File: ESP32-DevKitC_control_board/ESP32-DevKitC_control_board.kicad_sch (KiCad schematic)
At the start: 1 part, among them U1 ESP32-DevKitC

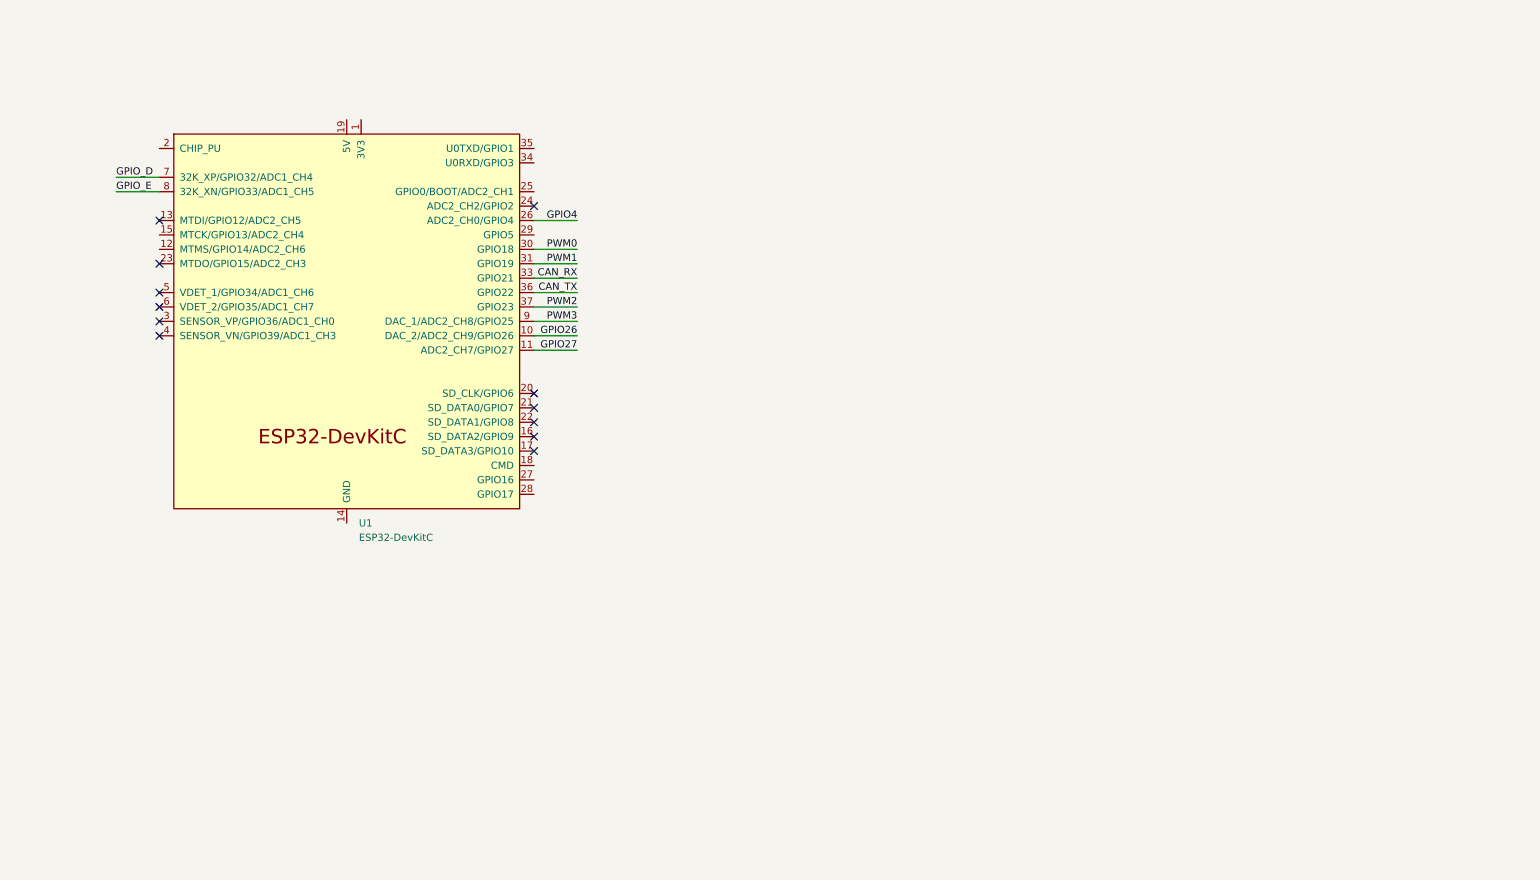
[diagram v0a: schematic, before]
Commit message: ESP32基板　回路図・フットプリント完成
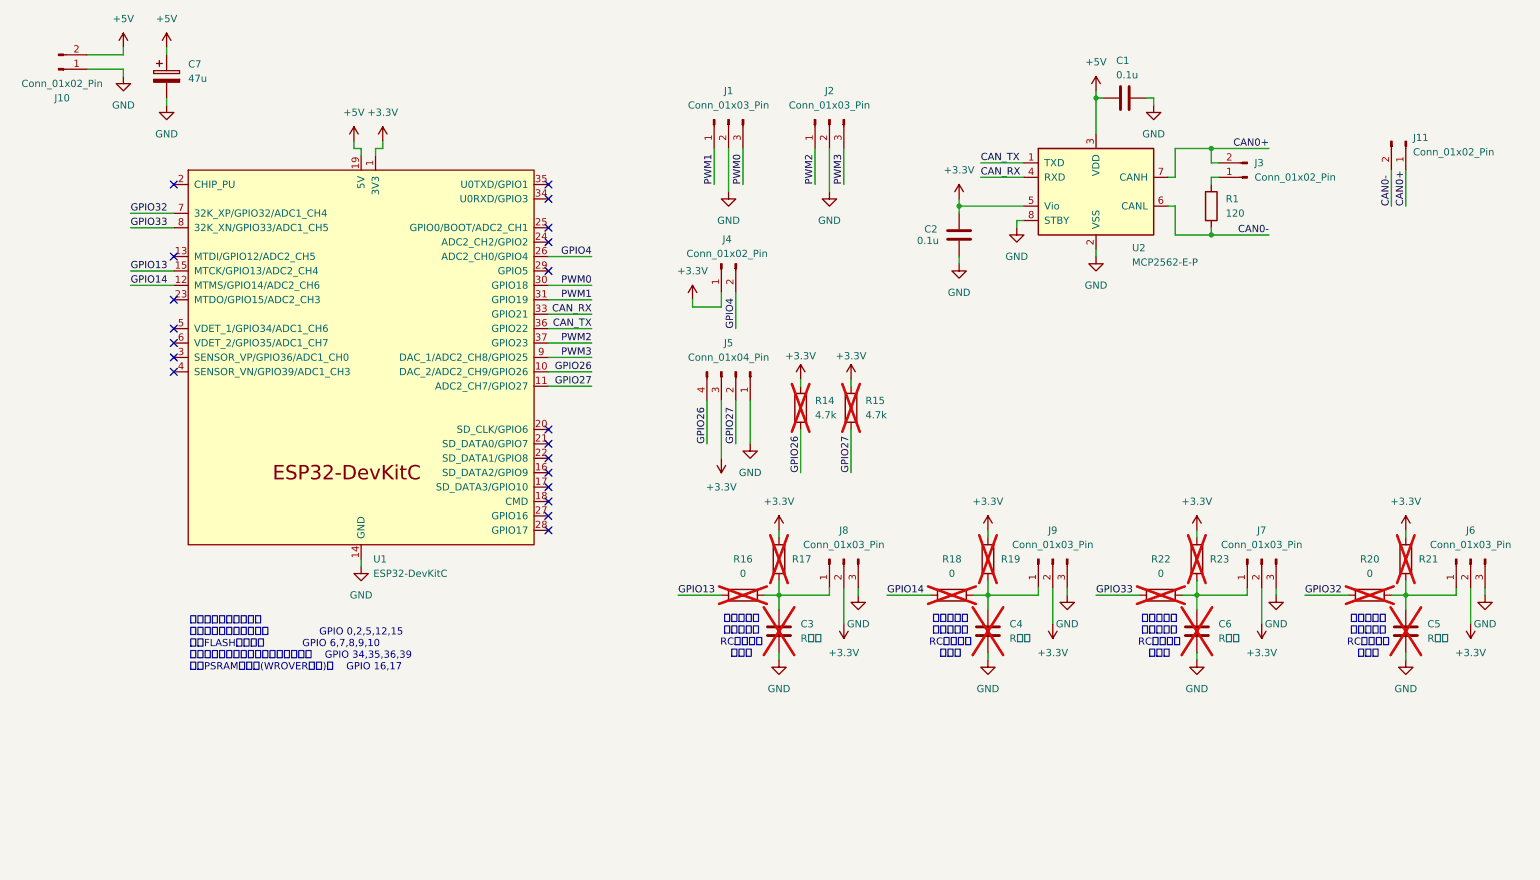
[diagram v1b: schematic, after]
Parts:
- added C1, C2: 0.1u, Capacitor_THT:C_Disc_D4.3mm_W1.9mm_P5.00mm, symbol Device:C
- added C3, C4, C5, C6: R兼用, Capacitor_THT:C_Disc_D3.8mm_W2.6mm_P2.50mm, symbol Device:C
- added C7: 47u, Capacitor_THT:CP_Radial_D6.3mm_P2.50mm, symbol Device:C_Polarized
- added J1, J2: Conn_01x03_Pin, OU_connector:S03B-PASK-2, symbol Connector:Conn_01x03_Pin
- added J10, J11, J4: Conn_01x02_Pin, OU_connector:DF1E-2P-2.5DS, symbol Connector:Conn_01x02_Pin
- added J3: Conn_01x02_Pin, Connector_PinHeader_2.54mm:PinHeader_1x02_P2.54mm_Vertical, symbol Connector:Conn_01x02_Pin
- added J5: Conn_01x04_Pin, OU_connector:DF1EC-4P-2.5DSA, symbol Connector:Conn_01x04_Pin
- added J6, J7, J8, J9: Conn_01x03_Pin, Connector_PinHeader_2.54mm:PinHeader_1x03_P2.54mm_Vertical, symbol Connector:Conn_01x03_Pin
- added R1: 120, Resistor_THT:R_Axial_DIN0204_L3.6mm_D1.6mm_P5.08mm_Horizontal, symbol Device:R
- added R14, R15: 4.7k, Resistor_THT:R_Axial_DIN0207_L6.3mm_D2.5mm_P2.54mm_Vertical, symbol Device:R
- added R16, R18, R20, R22: 0, Resistor_THT:R_Axial_DIN0207_L6.3mm_D2.5mm_P2.54mm_Vertical, symbol Device:R
- added R17, R19, R21, R23: (no value), Resistor_THT:R_Axial_DIN0207_L6.3mm_D2.5mm_P2.54mm_Vertical, symbol Device:R
- added U2: MCP2562-E-P, Package_DIP:DIP-8_W7.62mm, symbol Interface_CAN_LIN:MCP2562-E-P
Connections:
- net CAN_RX: now also U2.4 (RXD)
- net CAN_TX: now also U2.1 (TXD)
- net GPIO26: now also J5.4 (Pin_4), R14.2
- net GPIO27: now also J5.2 (Pin_2), R15.2
- net GPIO4: now also J4.2 (Pin_2)
- net PWM0: now also J1.3 (Pin_3)
- net PWM1: now also J1.1 (Pin_1)
- net PWM2: now also J2.1 (Pin_1)
- net PWM3: now also J2.3 (Pin_3)
- net +3.3V: now reaches U1.1 (3V3)
- net +3.3V: now also C2.2, J4.1 (Pin_1), J5.3 (Pin_3), J6.2 (Pin_2), J7.2 (Pin_2), J8.2 (Pin_2), J9.2 (Pin_2), R14.1, R15.1, R17.2, R19.2, R21.2, R23.2, U2.5 (Vio)
- net GPIO14: now reaches U1.12 (MTMS/GPIO14/ADC2_CH6)
- net GPIO14: now also R18.1
- net GND: now reaches U1.14 (GND), U1.32 (GND), U1.38 (GND)
- net GND: now also C1.2, C2.1, C3.2, C4.2, C5.2, C6.2, C7.2, J1.2 (Pin_2), J10.1 (Pin_1), J2.2 (Pin_2), J5.1 (Pin_1), J6.3 (Pin_3), J7.3 (Pin_3), J8.3 (Pin_3), J9.3 (Pin_3), U2.2 (VSS), U2.8 (STBY)
- net GPIO13: now reaches U1.15 (MTCK/GPIO13/ADC2_CH4)
- net GPIO13: now also R16.1
- net +5V: now reaches U1.19 (5V)
- net +5V: now also C1.1, C7.1, J10.2 (Pin_2), U2.3 (VDD)
- net GPIO_D renamed GPIO32
- net GPIO32: now also R20.1
- net GPIO_E renamed GPIO33
- net GPIO33: now also R22.1
- new net: C6.1, J7.1 (Pin_1), R22.2, R23.1
- new net: C3.1, J8.1 (Pin_1), R16.2, R17.1
- new net: C4.1, J9.1 (Pin_1), R18.2, R19.1
- new net: C5.1, J6.1 (Pin_1), R20.2, R21.1
- new net: J3.1 (Pin_1), R1.1
- new net CAN0+: J11.1 (Pin_1), J3.2 (Pin_2), U2.7 (CANH)
- new net CAN0-: J11.2 (Pin_2), R1.2, U2.6 (CANL)
- no-connect marks 12 -> 20
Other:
- note added: "プルアップ プルダウン RCフィルタ に対応"
- note added: "使わない方がいいピン ブートストラップピン： GPIO 0,2,5,12,15 内蔵FLASHで使用： GPIO 6,7,8,9,10 入力専用・プルアップ・ダウン不可： GPIO 34,35,36,39 外部PSRAMで使用(WROVERのみ)： GPIO 16,17"
- moved on the sheet: U1

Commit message: ESP32基板　PCB途中
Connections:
- net PWM0: now also U1.31 (GPIO19); no longer U1.30 (GPIO18)
- net PWM1: now also U1.30 (GPIO18); no longer U1.31 (GPIO19)

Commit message: ESP32基板　基板完成，ver 0.1
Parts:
- added D4: LED, LED_THT:LED_D5.0mm, symbol Device:LED
- added R12: 1k, Resistor_THT:R_Axial_DIN0207_L6.3mm_D2.5mm_P2.54mm_Vertical, symbol Device:R
- C2: renamed from C1; footprint Capacitor_THT:C_Disc_D4.3mm_W1.9mm_P5.00mm -> Capacitor_THT:C_Disc_D5.0mm_W2.5mm_P2.50mm
- C3: renamed from C2; footprint Capacitor_THT:C_Disc_D4.3mm_W1.9mm_P5.00mm -> Capacitor_THT:C_Disc_D5.0mm_W2.5mm_P2.50mm
- J10: renamed from J7; now not fitted
- J11: renamed from J6; now not fitted
- J7: renamed from J5; footprint OU_connector:DF1EC-4P-2.5DSA -> OU_connector:DF1E-4P-2.5DS
- J8, J9: now not fitted
- R1: footprint Resistor_THT:R_Axial_DIN0204_L3.6mm_D1.6mm_P5.08mm_Horizontal -> Resistor_THT:R_Axial_DIN0207_L6.3mm_D2.5mm_P2.54mm_Vertical
- renumbered C7 to C1, C3 to C4, C4 to C5, C5 to C7, J10 to J1, J1 to J2, J2 to J3, J11 to J4, J3 to J5, J4 to J6, R22 to R10, R20 to R11, R14 to R2, R15 to R3, R17 to R4, R19 to R5, R23 to R6, R21 to R7, R16 to R8, R18 to R9, U2 to U1, U1 to U2
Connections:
- net +5V: now also R12.1
- net CAN_RX: now also U2.30 (GPIO18); no longer U2.33 (GPIO21)
- net CAN_TX: now also U2.31 (GPIO19); no longer U2.36 (GPIO22)
- net GND: now also D4.1 (K)
- net PWM0: now also U2.12 (MTMS/GPIO14/ADC2_CH6); no longer U2.31 (GPIO19)
- net PWM1: now also U2.11 (ADC2_CH7/GPIO27); no longer U2.30 (GPIO18)
- net PWM2: now also U2.9 (DAC_1/ADC2_CH8/GPIO25); no longer U2.37 (GPIO23)
- net PWM3: now also U2.10 (DAC_2/ADC2_CH9/GPIO26); no longer U2.9 (DAC_1/ADC2_CH8/GPIO25)
- net GPIO14 renamed GPIO23
- net GPIO23: now also U2.37 (GPIO23); no longer U2.12 (MTMS/GPIO14/ADC2_CH6)
- net GPIO26 renamed GPIO21
- net GPIO21: now also U2.33 (GPIO21); no longer U2.10 (DAC_2/ADC2_CH9/GPIO26)
- net GPIO27 renamed GPIO22
- net GPIO22: now also U2.36 (GPIO22); no longer U2.11 (ADC2_CH7/GPIO27)
- new net: D4.2 (A), R12.2
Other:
- note added: "5V電源LED"
- moved on the sheet: C1, U2

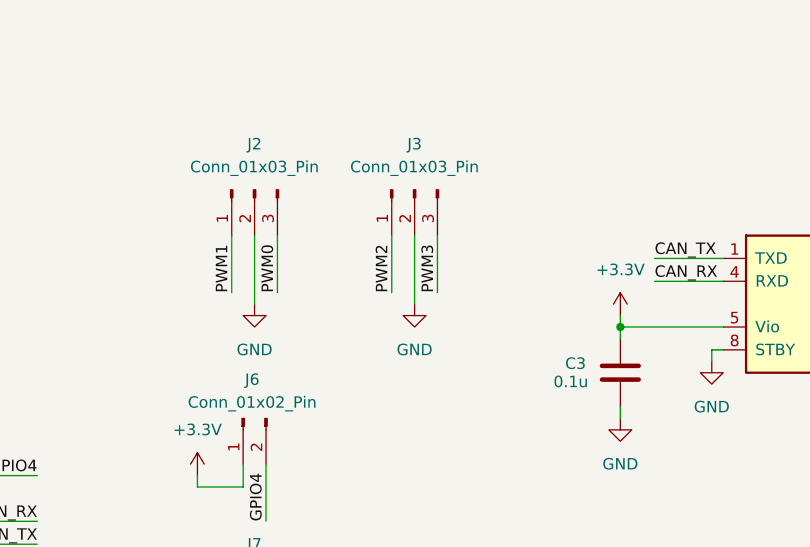
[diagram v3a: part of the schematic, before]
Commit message: ESP32基板　回路図を修正
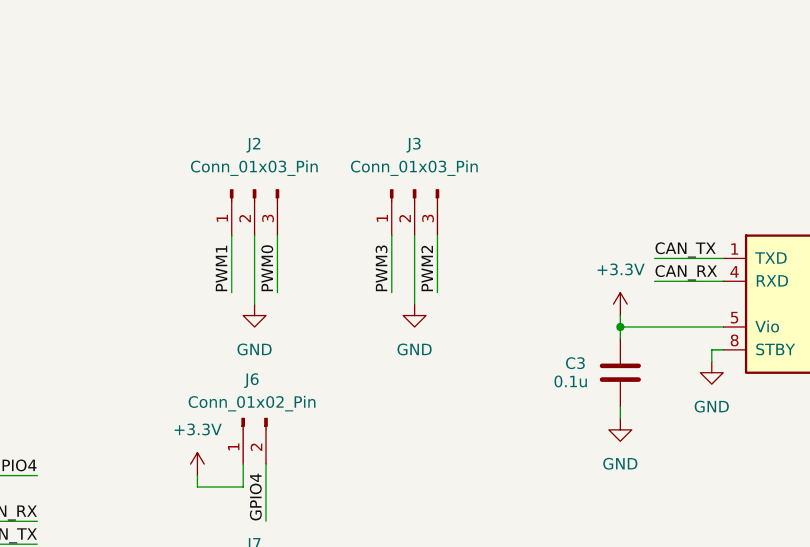
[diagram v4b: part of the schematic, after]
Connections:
- net PWM2: now also J3.3 (Pin_3); no longer J3.1 (Pin_1)
- net PWM3: now also J3.1 (Pin_1); no longer J3.3 (Pin_3)
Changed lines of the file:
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@@
-	(wire
-		(pts
-			(xy 154.94 44.45) (xy 154.94 38.1)
-		)
-		(stroke
-			(width 0)
-			(type default)
-		)
-	)
 	(wire
 		(pts
@@
 	(wire
 		(pts
+			(xy 154.94 38.1) (xy 154.94 44.45)
+		)
+		(stroke
+			(width 0)
+			(type default)
+		)
+	)
+	(wire
+		(pts
 			(xy 148.59 114.3) (xy 148.59 116.84)
 		)
@@
 	(wire
 		(pts
+			(xy 160.02 44.45) (xy 160.02 38.1)
+		)
+		(stroke
+			(width 0)
+			(type default)
+		)
+	)
+	(wire
+		(pts
 			(xy 236.22 115.57) (xy 236.22 116.84)
 		)
@@
 		(pts
 			(xy 148.59 128.27) (xy 148.59 127)
-		)
-		(stroke
-			(width 0)
-			(type default)
-		)
-	)
-	(wire
-		(pts
-			(xy 160.02 44.45) (xy 160.02 38.1)
 		)
 		(stroke
@@
 	)
 	(label "PWM3"
-		(at 160.02 44.45 90)
+		(at 154.94 44.45 90)
 		(effects
 			(font
@@
 	)
 	(label "PWM2"
-		(at 154.94 44.45 90)
+		(at 160.02 44.45 90)
 		(effects
 			(font

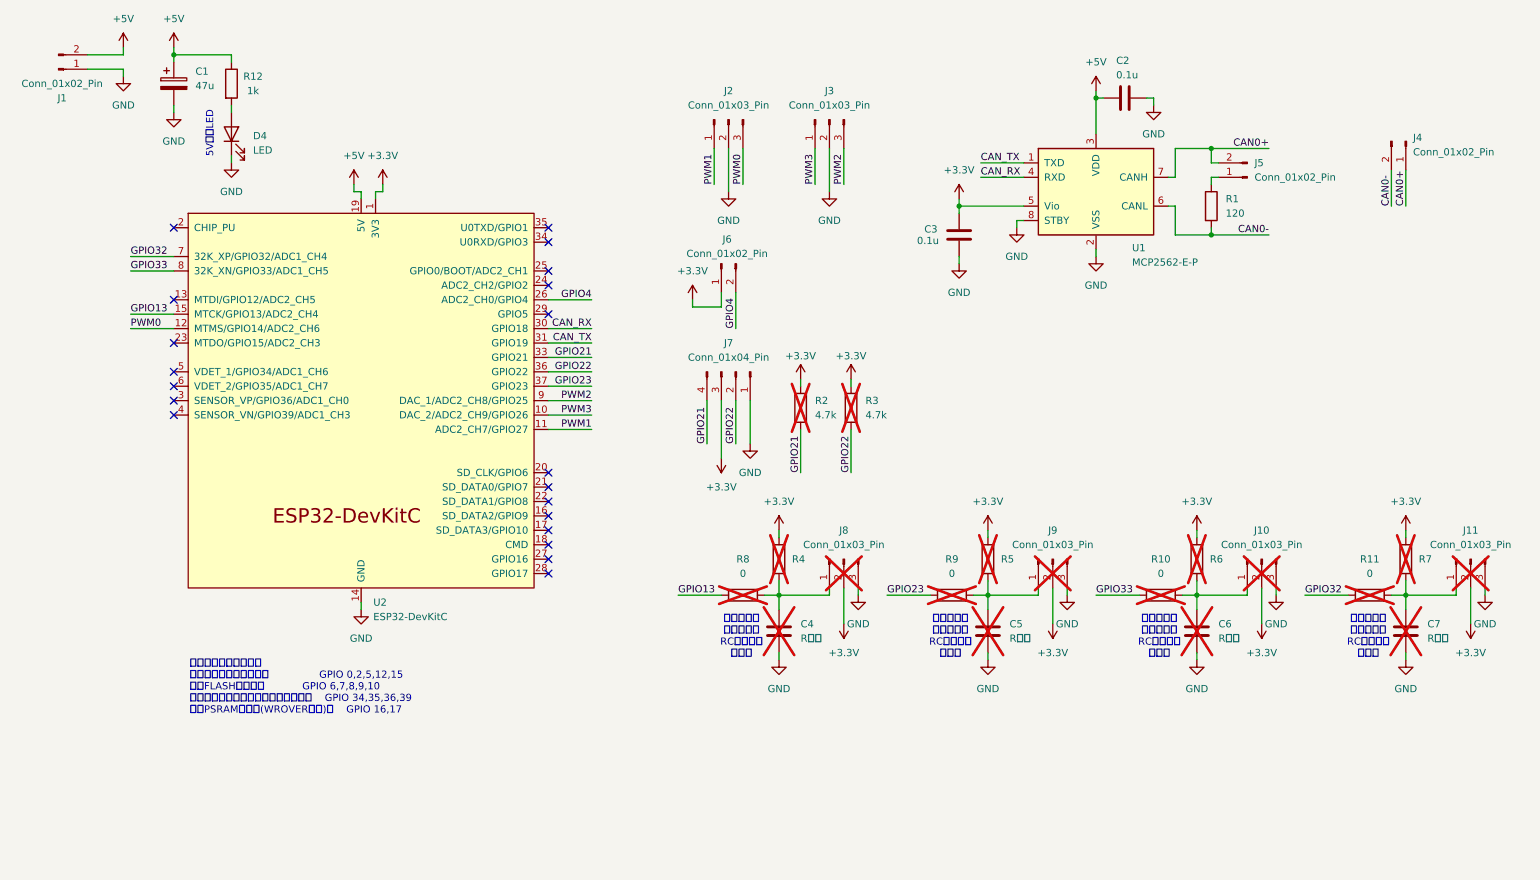
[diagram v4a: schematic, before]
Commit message: ESP32基板　回路図を見やすく修正
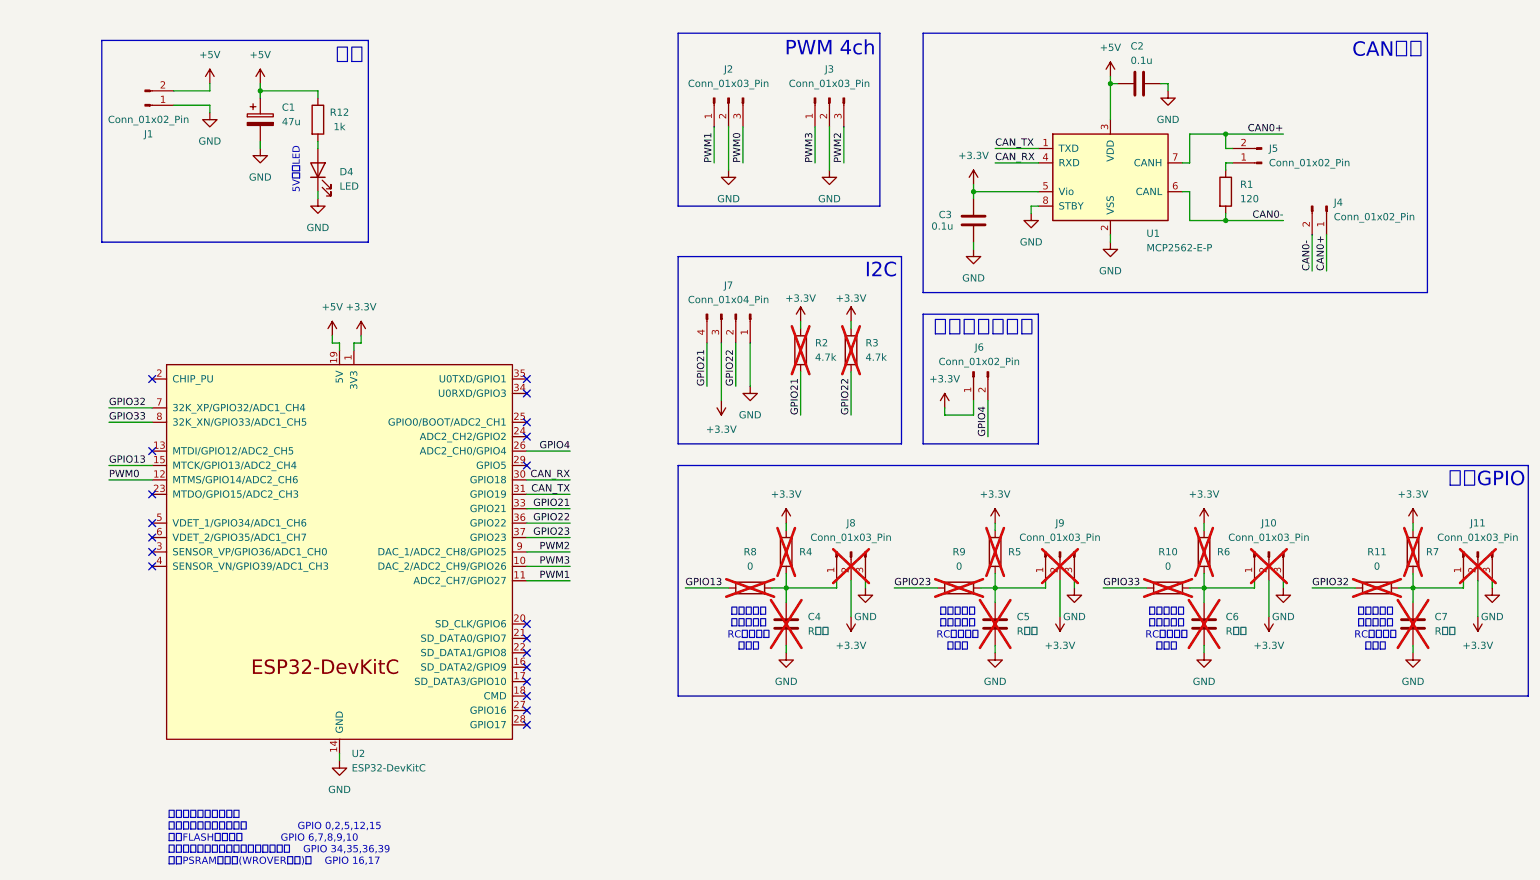
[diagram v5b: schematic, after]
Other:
- note added: "CAN通信"
- note added: "I2C"
- note added: "PWM 4ch"
- note added: "シリアルサーボ"
- note added: "予備GPIO"
- note added: "電源"
- moved on the sheet: C1, C2, C3, C4, C5, C6, C7, D4, J1, J10, J11, J2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

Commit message: ESP32基板　CAN0をCAN1に改名，ver 0.3 STMの場合，CANの通し番号は1からっぽい．
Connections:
- net CAN0+ renamed CAN1+
- net CAN0- renamed CAN1-
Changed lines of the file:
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@@
 		)
 	)
-	(label "CAN0+"
+	(label "CAN1+"
 		(at 237.49 35.56 180)
 		(effects
@@
 		)
 	)
-	(label "CAN0-"
+	(label "CAN1-"
 		(at 242.57 59.69 90)
 		(effects
@@
 		)
 	)
-	(label "CAN0+"
+	(label "CAN1+"
 		(at 245.11 59.69 90)
 		(effects
@@
 		)
 	)
-	(label "CAN0-"
+	(label "CAN1-"
 		(at 237.49 50.8 180)
 		(effects

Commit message: ESP32基板　I2C部分のネットラベル名を変更
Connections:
- net GPIO21 renamed I2C_SDA
- net GPIO22 renamed I2C_SCL
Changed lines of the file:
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@@
-		)
-	)
-	(label "GPIO22"
-		(at 111.76 104.14 180)
-		(effects
-			(font
-				(size 1.27 1.27)
-			)
-			(justify right bottom)
 		)
 	)
@@
 		)
 	)
+	(label "I2C_SDA"
+		(at 152.4 85.09 90)
+		(effects
+			(font
+				(size 1.27 1.27)
+			)
+			(justify left bottom)
+		)
+	)
 	(label "PWM3"
 		(at 154.94 40.64 90)
@@
 		)
 	)
+	(label "I2C_SCL"
+		(at 111.76 104.14 180)
+		(effects
+			(font
+				(size 1.27 1.27)
+			)
+			(justify right bottom)
+		)
+	)
 	(label "PWM0"
 		(at 30.48 96.52 0)
@@
 		)
 	)
-	(label "GPIO21"
-		(at 111.76 101.6 180)
-		(effects
-			(font
-				(size 1.27 1.27)
-			)
-			(justify right bottom)
-		)
-	)
 	(label "PWM0"
 		(at 142.24 40.64 90)
@@
 		)
 	)
+	(label "I2C_SDA"
+		(at 111.76 101.6 180)
+		(effects
+			(font
+				(size 1.27 1.27)
+			)
+			(justify right bottom)
+		)
+	)
 	(label "GPIO33"
 		(at 205.74 115.57 0)
@@
 		)
 	)
-	(label "GPIO21"
+	(label "I2C_SDA"
 		(at 135.89 80.01 90)
 		(effects
@@
 		)
 	)
-	(label "GPIO22"
-		(at 161.29 85.09 90)
-		(effects
-			(font
-				(size 1.27 1.27)
-			)
-			(justify left bottom)
-		)
-	)
 	(label "GPIO13"
 		(at 30.48 93.98 0)
@@
 		)
 	)
-	(label "GPIO22"
+	(label "I2C_SCL"
 		(at 140.97 80.01 90)
 		(effects
@@
 		)
 	)
-	(label "GPIO21"
-		(at 152.4 85.09 90)
-		(effects
-			(font
+	(label "I2C_SCL"
+		(at 161.29 85.09 90)
+		(effects
+			(font

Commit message: ESP32基板　PWMの通し番号も1スタートに変更，ver 0.4
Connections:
- net PWM0 is gone; now on net PWM1: J2.3 (Pin_3), U2.12 (MTMS/GPIO14/ADC2_CH6)
- net PWM1: no longer J2.1 (Pin_1), U2.11 (ADC2_CH7/GPIO27)
- net PWM2: now also J2.1 (Pin_1), U2.11 (ADC2_CH7/GPIO27); no longer J3.3 (Pin_3), U2.9 (DAC_1/ADC2_CH8/GPIO25)
- net PWM3: now also J3.3 (Pin_3), U2.9 (DAC_1/ADC2_CH8/GPIO25); no longer J3.1 (Pin_1), U2.10 (DAC_2/ADC2_CH9/GPIO26)
- new net PWM4: J3.1 (Pin_1), U2.10 (DAC_2/ADC2_CH9/GPIO26)
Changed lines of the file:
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@@
 		)
 	)
-	(label "PWM3"
+	(label "PWM4"
 		(at 154.94 40.64 90)
 		(effects
@@
 		)
 	)
-	(label "PWM1"
+	(label "PWM2"
 		(at 111.76 114.3 180)
 		(effects
@@
 		)
 	)
-	(label "PWM0"
+	(label "PWM1"
 		(at 30.48 96.52 0)
 		(effects
@@
 		)
 	)
-	(label "PWM0"
+	(label "PWM1"
 		(at 142.24 40.64 90)
 		(effects
@@
 		)
 	)
+	(label "PWM4"
+		(at 111.76 111.76 180)
+		(effects
+			(font
+				(size 1.27 1.27)
+			)
+			(justify right bottom)
+		)
+	)
 	(label "PWM3"
-		(at 111.76 111.76 180)
-		(effects
-			(font
-				(size 1.27 1.27)
-			)
-			(justify right bottom)
-		)
-	)
-	(label "PWM2"
 		(at 160.02 40.64 90)
 		(effects
@@
 		)
 	)
-	(label "PWM1"
+	(label "PWM2"
 		(at 137.16 40.64 90)
 		(effects
@@
 		)
 	)
-	(label "PWM2"
+	(label "PWM3"
 		(at 111.76 109.22 180)
 		(effects
